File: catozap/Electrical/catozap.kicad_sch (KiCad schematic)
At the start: 13 parts, among them J1 Out1, J2 Out1, J3 GPIO_In, J4 GPIO_In, J5 Out1, J6 GPIO_In, J7 GPIO_Gnd, Q1 NPN, Q2 NPN, Q3 NPN

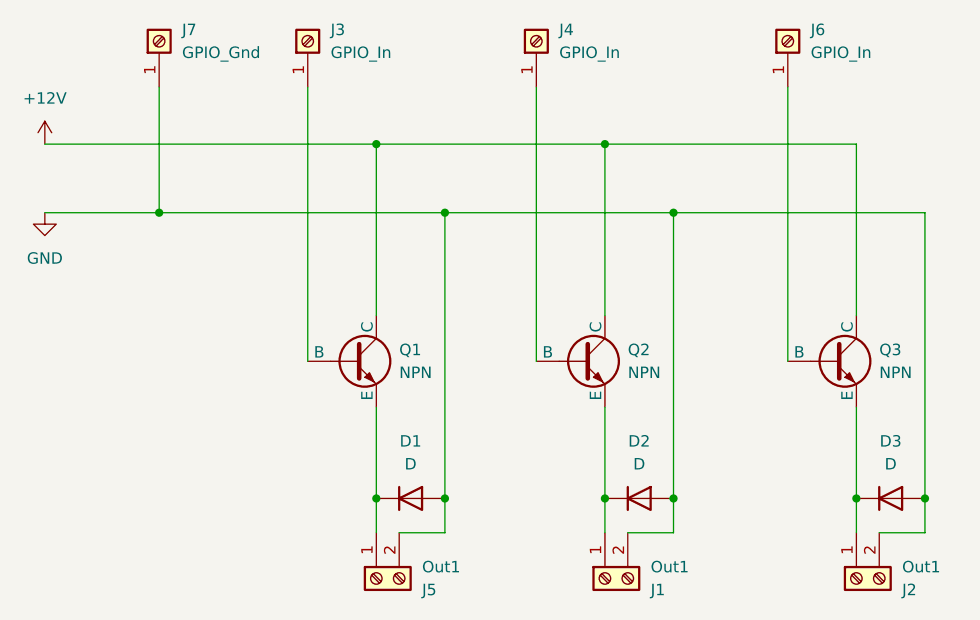
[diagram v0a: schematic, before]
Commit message: Changed catozap to common emitter configuration
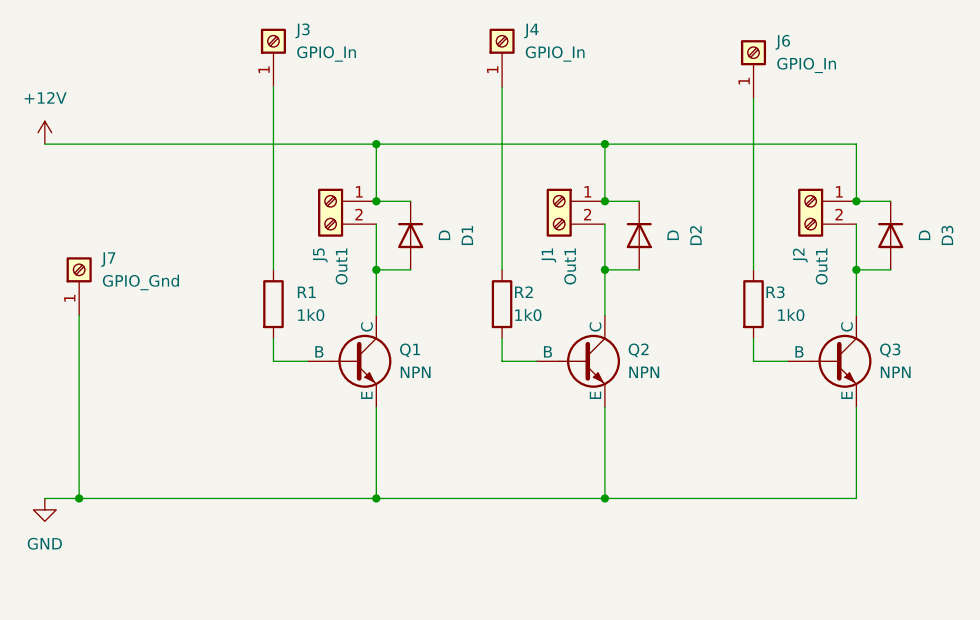
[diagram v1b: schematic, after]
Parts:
- added R1, R2, R3: 1k0, symbol Device:R
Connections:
- net +12V: now also D1.1 (K), D2.1 (K), D3.1 (K), J1.1 (Pin_1), J2.1 (Pin_1), J5.1 (Pin_1); no longer Q1.1 (C), Q2.1 (C), Q3.1 (C)
- net GND: now also Q1.3 (E), Q2.3 (E), Q3.3 (E); no longer D1.2 (A), D2.2 (A), D3.2 (A), J1.2 (Pin_2), J2.2 (Pin_2), J5.2 (Pin_2)
- net at J6.1 (Pin_1): now also R3.1; no longer Q3.2 (B)
- net at J4.1 (Pin_1): now also R2.1; no longer Q2.2 (B)
- net at J3.1 (Pin_1): now also R1.1; no longer Q1.2 (B)
- new net: D3.2 (A), J2.2 (Pin_2), Q3.1 (C)
- new net: D2.2 (A), J1.2 (Pin_2), Q2.1 (C)
- new net: Q3.2 (B), R3.2
- new net: Q2.2 (B), R2.2
- new net: Q1.2 (B), R1.2
- new net: D1.2 (A), J5.2 (Pin_2), Q1.1 (C)
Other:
- moved on the sheet: D1, D2, D3, J1, J2, J3, J4, J5, J6, J7

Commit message: Update to elecrical schematic
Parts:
- removed Q1, Q2, Q3: NPN, symbol Simulation_SPICE:NPN
- added Q4, Q5, Q6: TIP120, Package_TO_SOT_THT:TO-220-3_Vertical, symbol Transistor_BJT:TIP120
- D1, D2, D3: footprint (none) -> Diode_THT:D_5KP_P7.62mm_Vertical_KathodeUp
- R1, R2, R3: footprint (none) -> Resistor_THT:R_Axial_DIN0207_L6.3mm_D2.5mm_P7.62mm_Horizontal
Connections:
- net GND: now also Q4.3 (E), Q5.3 (E), Q6.3 (E)
- net at D3.2 (A), J2.2 (Pin_2): now also Q6.2 (C)
- net at D2.2 (A), J1.2 (Pin_2): now also Q5.2 (C)
- net at R3.2: now also Q6.1 (B)
- net at R2.2: now also Q5.1 (B)
- net at R1.2: now also Q4.1 (B)
- net at D1.2 (A), J5.2 (Pin_2): now also Q4.2 (C)
